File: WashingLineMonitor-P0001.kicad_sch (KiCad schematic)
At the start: 3 parts

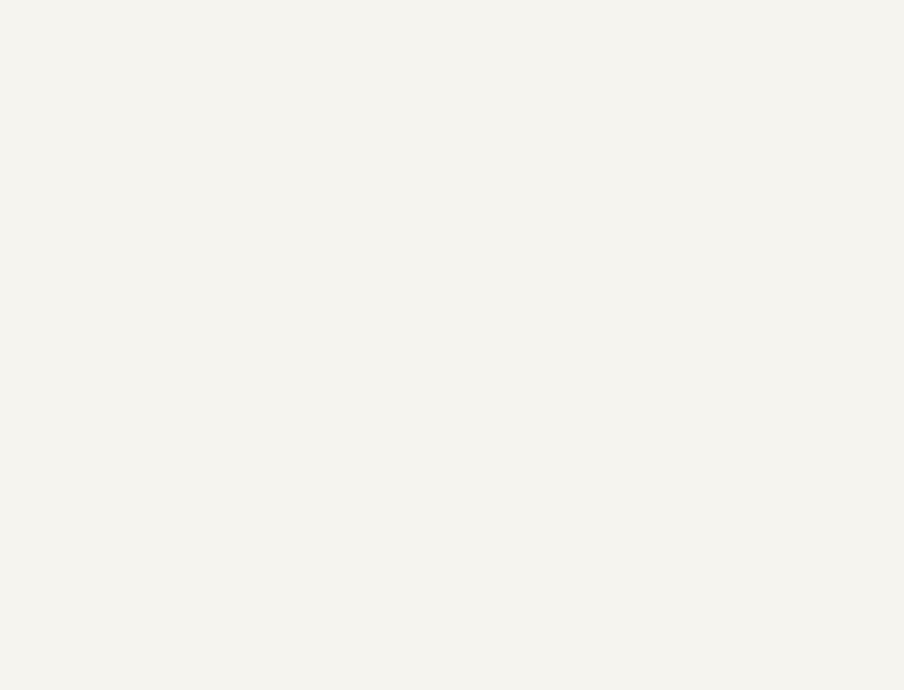
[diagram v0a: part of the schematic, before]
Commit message: Added boot pin strapping
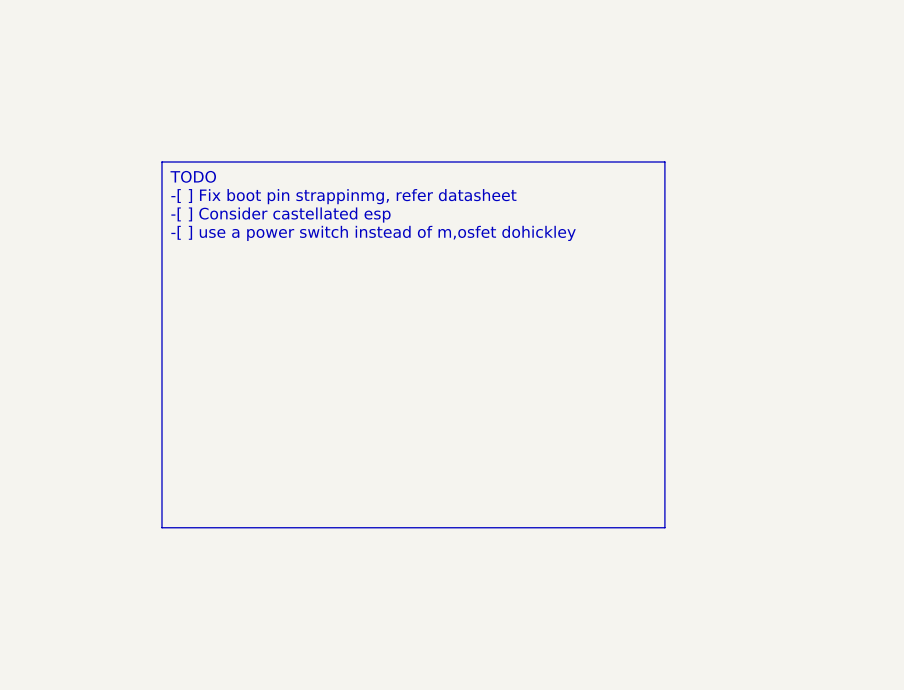
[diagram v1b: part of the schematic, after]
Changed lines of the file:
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@@
 		(comment 3 "AC - Added Connector, Switch to ESP32 C3, added humidity sensor and power switch")
+	)
+	(text_box "TODO\n-[ ] Fix boot pin strappinmg, refer datasheet\n-[ ] Consider castellated esp\n-[ ] use a power switch instead of m,osfet dohickley"
+		(exclude_from_sim no)
+		(at 54.61 77.47 0)
+		(size 55.88 40.64)
+		(margins 0.9525 0.9525 0.9525 0.9525)
+		(stroke
+			(width 0)
+			(type solid)
+		)
+		(fill
+			(type none)
+		)
+		(effects
+			(font
+				(size 1.27 1.27)
+			)
+			(justify left top)
+		)
 	)
 	(symbol

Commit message: finished board layout for AD revision
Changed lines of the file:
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@@
 		(comment 1 "AA - Original")
 		(comment 2 "AB - Updated from AI review")
-		(comment 3 "AC - Added Connector, Switch to ESP32 C3, added humidity sensor and power switch")
-	)
-	(text_box "TODO\n-[ ] Fix boot pin strappinmg, refer datasheet\n-[ ] Consider castellated esp\n-[ ] use a power switch instead of m,osfet dohickley"
-		(exclude_from_sim no)
-		(at 54.61 77.47 0)
-		(size 55.88 40.64)
-		(margins 0.9525 0.9525 0.9525 0.9525)
-		(stroke
-			(width 0)
-			(type solid)
-		)
-		(fill
-			(type none)
-		)
-		(effects
-			(font
-				(size 1.27 1.27)
-			)
-			(justify left top)
-		)
+		(comment 3 "AC - Added Connector, Switch to ESP32 C6, added humidity sensor and power switch")
+		(comment 4 "AD - Fixed issue with ESP boot pin, switched to new large esp package, replaced mosfet with power switch")
 	)
 	(symbol
